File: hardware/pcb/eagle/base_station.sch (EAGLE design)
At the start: 105 parts, among them CON1 RJ45-8PTH, CON2 RJ45-8PTH, CON3 RJ45-8PTH, CON4 RJ45-8PTH, CON5 RJ45-8PTH, CON6 RJ45-8PTH, CON7 RJ45-8PTH, CON8 RJ45-8PTH, IC1 LTC2851S, IC10 LTC2851S, IC11 LTC2851S, IC12 LTC2851S, IC13 LTC2851S, IC14 LTC2851S, IC15 LTC2851S, IC16 LTC2851S, IC17 NC7WZ16P6X, IC18 7Q-16.368MBG-T, IC19 LTC2851S, IC2 LTC2851S, IC20 LTC2851S, IC21 LTC2851S, IC22 LTC2851S, IC23 LTC2851S, IC24 LTC2851S, IC25 LTC2851S, IC26 LTC2851S, IC3 LTC2851S, IC4 LTC2851S, IC5 LTC2851S, IC6 LTC2851S, IC7 LTC2851S, IC8 LTC2851S, IC9 LTC2851S

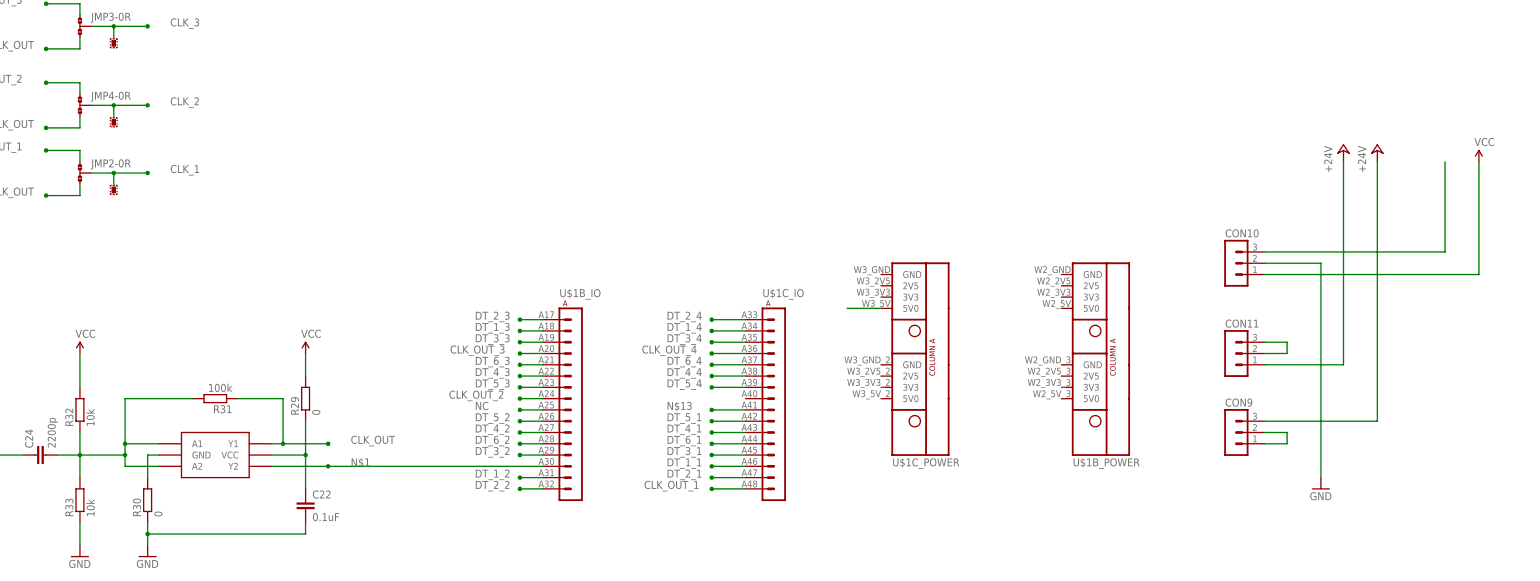
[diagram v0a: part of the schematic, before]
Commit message: Changes to oscillator circuit. Added RJ45 for SPI
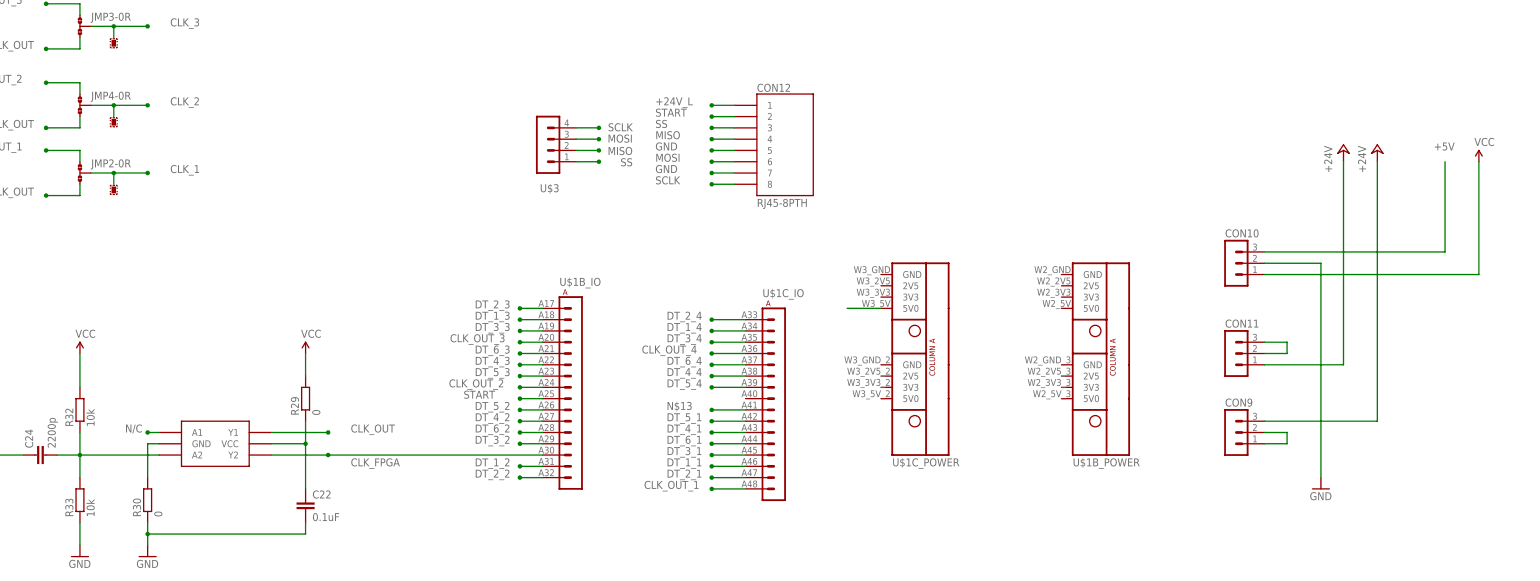
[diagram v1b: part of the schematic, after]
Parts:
- removed R31: 100k, rcl:R-EU_R0603
- added CON12: RJ45-8PTH, SparkFun:RJ45-8PTH
- added U$3: WING4, Papilio:WING4
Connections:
- net N$1 renamed CLK_FPGA
- removed net NC: U$1B_IO.A9
- new net MISO: CON12.4, U$3.A2
- new net MOSI: CON12.6, U$3.A3
- new net N/C: IC17.A1@1
- new net SCLK: CON12.8, U$3.A4
- new net SS: CON12.3, U$3.A1
- new net START: CON12.2, U$1B_IO.A9
- net +24V_L: now also CON12.1
- net CLK_OUT: no longer R31.1
- net GND: now also CON12.5, CON12.7
- net N$6: no longer IC17.A1@1, R31.2
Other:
- moved on the sheet: U$1B_IO

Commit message: Added silk screen layers, and ammended component names to suit
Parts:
- removed IC25: LTC2851S, texas_lvds:LTC2851S
- added X1: 7Q-16.368MBG-T, texas_lvds:7Q-16.368MBG-T
- C24: value 2200p -> 0.1uF
- C26: value 0.1uF -> 2200p
- IC17: value NC7WZ16P6X -> LTC2851S; device texas_lvds:NC7WZ16P6X -> texas_lvds:LTC2851S
- IC18: value 7Q-16.368MBG-T -> LTC2851S; device texas_lvds:7Q-16.368MBG-T -> texas_lvds:LTC2851S
- IC26: value LTC2851S -> NC7WZ16P6X; device texas_lvds:LTC2851S -> texas_lvds:NC7WZ16P6X
- renumbered R33 to R31, U$1 to CON14, U$3 to CON13
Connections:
- net CLK_1: now also JMP1-0R.2; no longer JMP2-0R.2
- net CLK_2: now also JMP2-0R.2; no longer JMP4-0R.2
- net CLK_4: now also IC20.DI, JMP4-0R.2; no longer IC22.DI, JMP1-0R.2
- net CLK_FPGA: now also IC26.Y2@4; no longer IC17.Y2@4
- net CLK_INV_2: now also R10.2; no longer R9.2
- net CLK_INV_3: now also R17.2; no longer R16.2
- net CLK_INV_4: now also IC20.Z, R24.2; no longer IC22.Z, R23.2
- net CLK_NINV_2: now also R10.1; no longer R9.1
- net CLK_NINV_3: now also R17.1; no longer R16.1
- net CLK_NINV_4: now also IC20.Y, R24.1; no longer IC22.Y, R23.1
- net CLK_OUT: now also IC26.Y1@6; no longer IC17.Y1@6
- net CLK_OUT_1: now also JMP1-0R.1; no longer JMP2-0R.1
- net CLK_OUT_2: now also JMP2-0R.1; no longer JMP4-0R.1
- net CLK_OUT_4: now also JMP4-0R.1; no longer JMP1-0R.1
- net DT_1_4: now also IC20.RO; no longer IC22.RO
- net DT_1_INV_2: now also R9.1; no longer R10.1
- net DT_1_INV_3: now also R16.1; no longer R17.1
- net DT_1_INV_4: now also IC20.A, R23.1; no longer IC22.A, R24.1
- net DT_1_NINV_2: now also R9.2; no longer R10.2
- net DT_1_NINV_3: now also R16.2; no longer R17.2
- net DT_1_NINV_4: now also IC20.B, R23.2; no longer IC22.B, R24.2
- net DT_2_2: now also IC9.RO; no longer IC7.RO
- net DT_2_3: now also IC15.RO; no longer IC13.RO
- net DT_2_INV_2: now also IC9.B, R11.1; no longer IC7.B, R8.1
- net DT_2_INV_3: now also IC15.B, R18.1; no longer IC13.B, R15.1
- net DT_2_INV_4: now also R25.1; no longer R22.1
- net DT_2_NINV_2: now also IC9.A, R11.2; no longer IC7.A, R8.2
- net DT_2_NINV_3: now also IC15.A, R18.2; no longer IC13.A, R15.2
- net DT_2_NINV_4: now also R25.2; no longer R22.2
- net DT_3_2: now also IC7.RO; no longer IC9.RO
- net DT_3_3: now also IC13.RO; no longer IC15.RO
- net DT_3_4: now also IC19.RO; no longer IC23.RO
- net DT_3_INV_2: now also IC7.B, R8.1; no longer IC9.B, R11.1
- net DT_3_INV_3: now also IC13.B, R15.1; no longer IC15.B, R18.1
- net DT_3_INV_4: now also IC19.B, R22.1; no longer IC23.B, R25.1
- net DT_3_NINV_2: now also IC7.A, R8.2; no longer IC9.A, R11.2
- net DT_3_NINV_3: now also IC13.A, R15.2; no longer IC15.A, R18.2
- net DT_3_NINV_4: now also IC19.A, R22.2; no longer IC23.A, R25.2
- net DT_4_3: now also IC17.RO; no longer IC19.RO
- net DT_4_4: now also IC23.RO; no longer IC25.RO
- net DT_4_INV_3: now also IC17.B; no longer IC19.B
- net DT_4_INV_4: now also IC23.B; no longer IC25.B
- net DT_4_NINV_3: now also IC17.A; no longer IC19.A
- net DT_4_NINV_4: now also IC23.A; no longer IC25.A
- net DT_5_2: now also IC12.RO; no longer IC10.RO
- net DT_5_3: now also IC18.RO; no longer IC16.RO
- net DT_5_INV_2: now also IC12.B, R14.1; no longer IC10.B, R12.1
- net DT_5_INV_3: now also IC18.B, R21.1; no longer IC16.B, R19.1
- net DT_5_INV_4: now also R28.1; no longer R26.1
- net DT_5_NINV_2: now also IC12.A, R14.2; no longer IC10.A, R12.2
- net DT_5_NINV_3: now also IC18.A, R21.2; no longer IC16.A, R19.2
- net DT_5_NINV_4: now also R28.2; no longer R26.2
- net DT_6_2: now also IC10.RO; no longer IC12.RO
- net DT_6_3: now also IC16.RO; no longer IC20.RO
- net DT_6_4: now also IC22.RO; no longer IC26.RO
- net DT_6_INV_2: now also IC10.B, R12.1; no longer IC12.B, R14.1
- net DT_6_INV_3: now also IC16.B, R19.1; no longer IC20.B, R21.1
- net DT_6_INV_4: now also IC22.B, R26.1; no longer IC26.B, R28.1
- net DT_6_NINV_2: now also IC10.A, R12.2; no longer IC12.A, R14.2
- net DT_6_NINV_3: now also IC16.A, R19.2; no longer IC20.A, R21.2
- net DT_6_NINV_4: now also IC22.A, R26.2; no longer IC26.A, R28.2
- net GND: now also C24.2, IC17.GND, IC18.DI, IC18.GND, IC19.DI, IC22.DI, X1.AFC/GND, X1.GND_2; no longer C26.2, IC18.AFC/GND, IC18.GND_2, IC20.DI, IC23.DI, IC25.GND, IC26.DI, IC26.GND
- net N$4: now also IC26.GND@2; no longer IC17.GND@2
- net N$5: now also C25.1, IC26.VCC@5; no longer C22.1, IC17.VCC@5
- net N$6: now also C26.2, IC26.A2@3; no longer C24.2, IC17.A2@3
- net N$9: now also C26.1, X1.OUT; no longer C24.1, IC18.OUT
- net N/C: now also IC26.A1@1; no longer IC17.A1@1
- net VCC: now also C22.1, C24.1, IC17.VCC, IC18.VCC, X1.VDD; no longer C25.1, C26.1, IC18.VDD, IC25.VCC, IC26.VCC
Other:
- moved on the sheet: C10, C12, C13, C15, C16, C18, C19, C21, C22, C23, C24, C25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
